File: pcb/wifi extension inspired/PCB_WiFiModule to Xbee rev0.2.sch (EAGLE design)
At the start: 20 parts, among them J1 FA12-1W, U1 XBP9B-DMUT-002

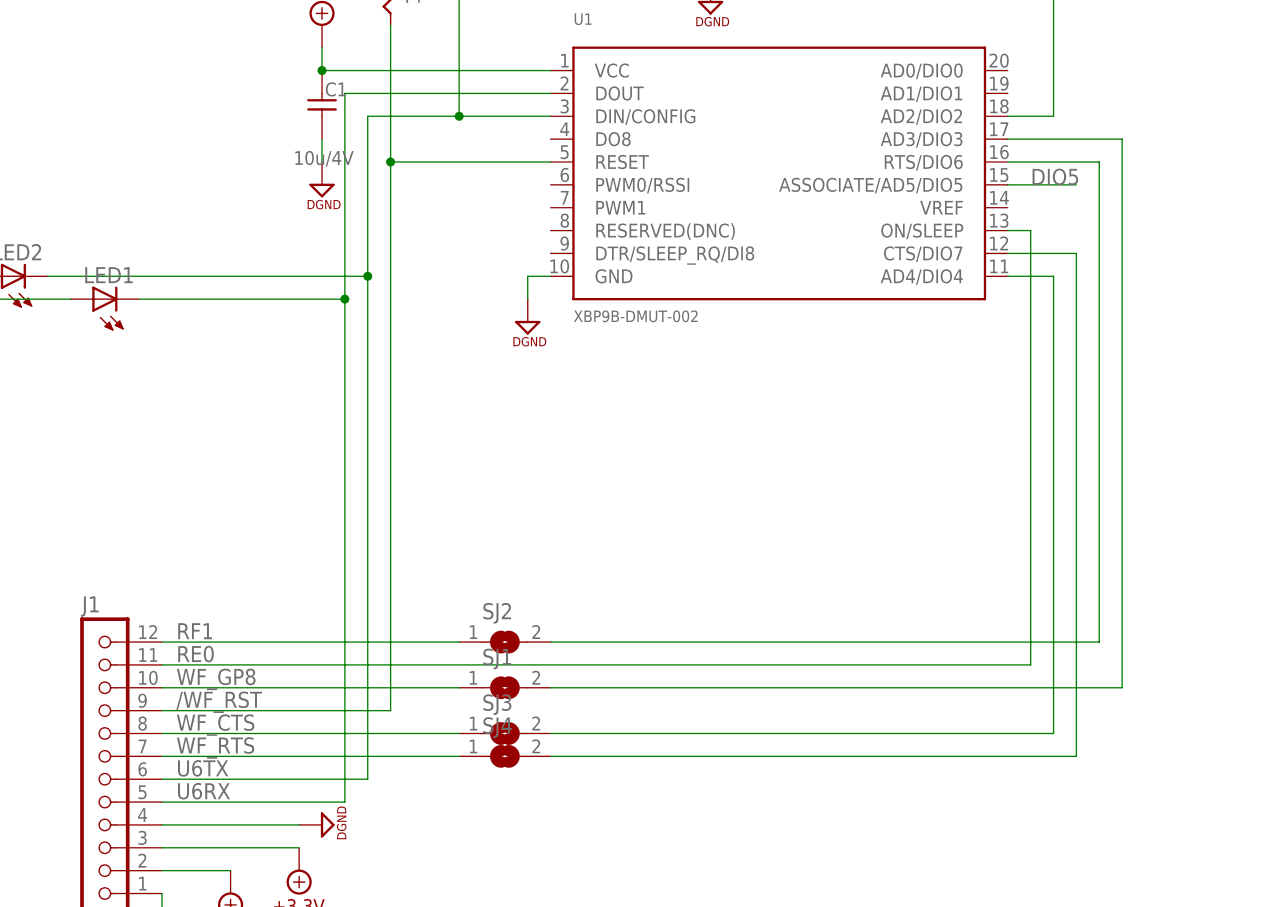
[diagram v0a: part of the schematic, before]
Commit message: cleaned up routing, rerouted some SJ to go to different GPIO on the Xbee module.
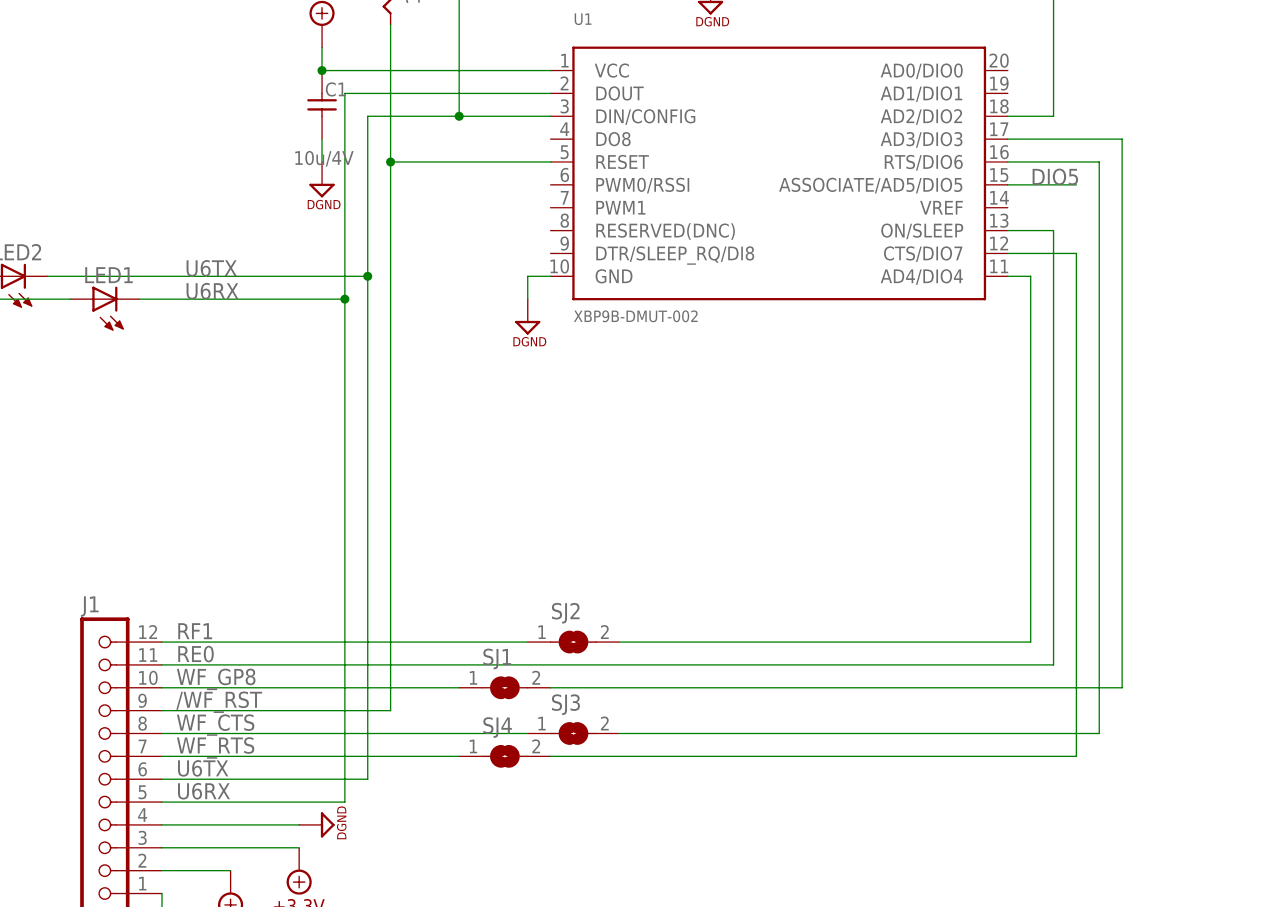
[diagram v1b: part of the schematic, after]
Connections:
- net N$10: now also SJ2.2; no longer SJ3.2
- net N$11: now also SJ3.2; no longer SJ2.2
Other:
- moved on the sheet: SJ2, SJ3
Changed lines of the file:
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@@
 <instance part="U$8" gate="G$1" x="137.16" y="218.44" smashed="yes"/>
 <instance part="SJ1" gate="1" x="149.86" y="132.08"/>
-<instance part="SJ2" gate="1" x="149.86" y="137.16"/>
-<instance part="SJ3" gate="1" x="149.86" y="127"/>
+<instance part="SJ2" gate="1" x="157.48" y="137.16"/>
+<instance part="SJ3" gate="1" x="157.48" y="127"/>
 <instance part="SJ4" gate="1" x="149.86" y="124.46"/>
 <instance part="R6" gate="G$1" x="165.1" y="213.36" smashed="yes" rot="R180">
@@
 <pinref part="J1" gate="G$1" pin="8"/>
 <pinref part="SJ3" gate="1" pin="1"/>
-<wire x1="111.76" y1="127" x2="144.78" y2="127" width="0.1524" layer="91"/>
+<wire x1="111.76" y1="127" x2="152.4" y2="127" width="0.1524" layer="91"/>
 </segment>
 </net>
@@
 <junction x="132.08" y="175.26"/>
 <pinref part="LED1" gate="G$1" pin="C"/>
+<label x="114.3" y="175.26" size="1.778" layer="95"/>
 </segment>
 </net>
@@
 <wire x1="144.78" y1="213.36" x2="149.86" y2="213.36" width="0.1524" layer="91"/>
 <junction x="144.78" y="195.58"/>
+<label x="114.3" y="177.8" size="1.778" layer="95"/>
 </segment>
 </net>
@@
 <segment>
 <label x="113.3475" y="134.9375" size="1.778" layer="95"/>
-<wire x1="111.76" y1="134.62" x2="208.28" y2="134.62" width="0.1524" layer="91"/>
+<wire x1="111.76" y1="134.62" x2="210.82" y2="134.62" width="0.1524" layer="91"/>
 <pinref part="J1" gate="G$1" pin="11"/>
 <pinref part="U1" gate="G$1" pin="ON/SLEEP"/>
-<wire x1="205.74" y1="182.88" x2="208.28" y2="182.88" width="0.1524" layer="91"/>
-<wire x1="208.28" y1="182.88" x2="208.28" y2="134.62" width="0.1524" layer="91"/>
+<wire x1="205.74" y1="182.88" x2="210.82" y2="182.88" width="0.1524" layer="91"/>
+<wire x1="210.82" y1="182.88" x2="210.82" y2="134.62" width="0.1524" layer="91"/>
 </segment>
 </net>
@@
 <pinref part="J1" gate="G$1" pin="12"/>
 <pinref part="SJ2" gate="1" pin="1"/>
-<wire x1="111.76" y1="137.16" x2="144.78" y2="137.16" width="0.1524" layer="91"/>
+<wire x1="111.76" y1="137.16" x2="152.4" y2="137.16" width="0.1524" layer="91"/>
 </segment>
 </net>
@@
 <pinref part="U1" gate="G$1" pin="CTS/DIO7"/>
 <wire x1="205.74" y1="180.34" x2="213.36" y2="180.34" width="0.1524" layer="91"/>
+<wire x1="213.36" y1="180.34" x2="213.36" y2="124.46" width="0.1524" layer="91"/>
 <pinref part="SJ4" gate="1" pin="2"/>
-<wire x1="213.36" y1="180.34" x2="213.36" y2="124.46" width="0.1524" layer="91"/>
 <wire x1="213.36" y1="124.46" x2="154.94" y2="124.46" width="0.1524" layer="91"/>
 </segment>
@@
 <segment>
 <pinref part="U1" gate="G$1" pin="AD4/DIO4"/>
-<wire x1="205.74" y1="177.8" x2="210.82" y2="177.8" width="0.1524" layer="91"/>
+<wire x1="205.74" y1="177.8" x2="208.28" y2="177.8" width="0.1524" layer="91"/>
+<wire x1="208.28" y1="177.8" x2="208.28" y2="137.16" width="0.1524" layer="91"/>
+<pinref part="SJ2" gate="1" pin="2"/>
+<wire x1="208.28" y1="137.16" x2="162.56" y2="137.16" width="0.1524" layer="91"/>
+</segment>
+</net>
+<net name="N$11" class="0">
+<segment>
+<pinref part="U1" gate="G$1" pin="RTS/DIO6"/>
+<wire x1="215.9" y1="127" x2="215.9" y2="190.5" width="0.1524" layer="91"/>
+<wire x1="215.9" y1="190.5" x2="205.74" y2="190.5" width="0.1524" layer="91"/>
 <pinref part="SJ3" gate="1" pin="2"/>
-<wire x1="210.82" y1="177.8" x2="210.82" y2="127" width="0.1524" layer="91"/>
-<wire x1="210.82" y1="127" x2="154.94" y2="127" width="0.1524" layer="91"/>
-</segment>
-</net>
-<net name="N$11" class="0">
-<segment>
-<pinref part="SJ2" gate="1" pin="2"/>
-<wire x1="154.94" y1="137.16" x2="215.9" y2="137.16" width="0.1524" layer="91"/>
-<wire x1="215.9" y1="137.16" x2="215.9" y2="190.5" width="0.1524" layer="91"/>
-<pinref part="U1" gate="G$1" pin="RTS/DIO6"/>
-<wire x1="215.9" y1="190.5" x2="205.74" y2="190.5" width="0.1524" layer="91"/>
-</segment>
-</net>
+<wire x1="162.56" y1="127" x2="215.9" y2="127" width="0.1524" layer="91"/>
+</segment>
+</net>
